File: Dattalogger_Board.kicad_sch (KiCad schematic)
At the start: 0 parts

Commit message: Have added required symbols to the schematic sheets.
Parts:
- added BT1: Battery, Connector_PinHeader_2.54mm:PinHeader_2x01_P2.54mm_Vertical, symbol Device:Battery
- added C1, C2, C3, C4: C, Capacitor_SMD:C_0805_2012Metric, symbol Device:C
- added C5: C_Polarized, symbol Device:C_Polarized
- added D1, D2: LED, LED_SMD:LED_0805_2012Metric, symbol Device:LED
- added R1, R2, R6: 10K, symbol Device:R
- added R3, R4: 4.7K, symbol Device:R
- added R5, R7: 330, symbol Device:R
- added U1: ATMEGA328P-AU, ATMEGA328P-AU:QFP80P900X900X120-32N, symbol ATMEGA328P-AU:ATMEGA328P-AU
- added U2: RV-3129-C3, RV-3129-C3:IC_RV-3129-C3, symbol RV-3129-C3:RV-3129-C3
- added U3, U4: 24LC1025, Package_SO:SOIC-8_5.23x5.23mm_P1.27mm, symbol Memory_EEPROM:24LC1025
- added Y1: 32.768 KHz, CC7V-T1A-100.000KHZ-9PF-100PPM-TA-QC:XTAL_CC7V-T1A-100.000KHZ-9PF-100PPM-TA-QC, symbol CC7V-T1A-100.000KHZ-9PF-100PPM-TA-QC:CC7V-T1A-100.000KHZ-9PF-100PPM-TA-QC
- added Y2: 16 MHz, CC7V-T1A-100.000KHZ-9PF-100PPM-TA-QC:XTAL_CC7V-T1A-100.000KHZ-9PF-100PPM-TA-QC, symbol CC7V-T1A-100.000KHZ-9PF-100PPM-TA-QC:CC7V-T1A-100.000KHZ-9PF-100PPM-TA-QC
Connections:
- new net: U2.10 (NC), U2.8 (NC)
- new net: U1.21 (GND), U1.3 (GND), U1.5 (GND)
- new net: U1.4 (VCC), U1.6 (VCC)
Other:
- added sheet Connectors (Connectors.kicad_sch)

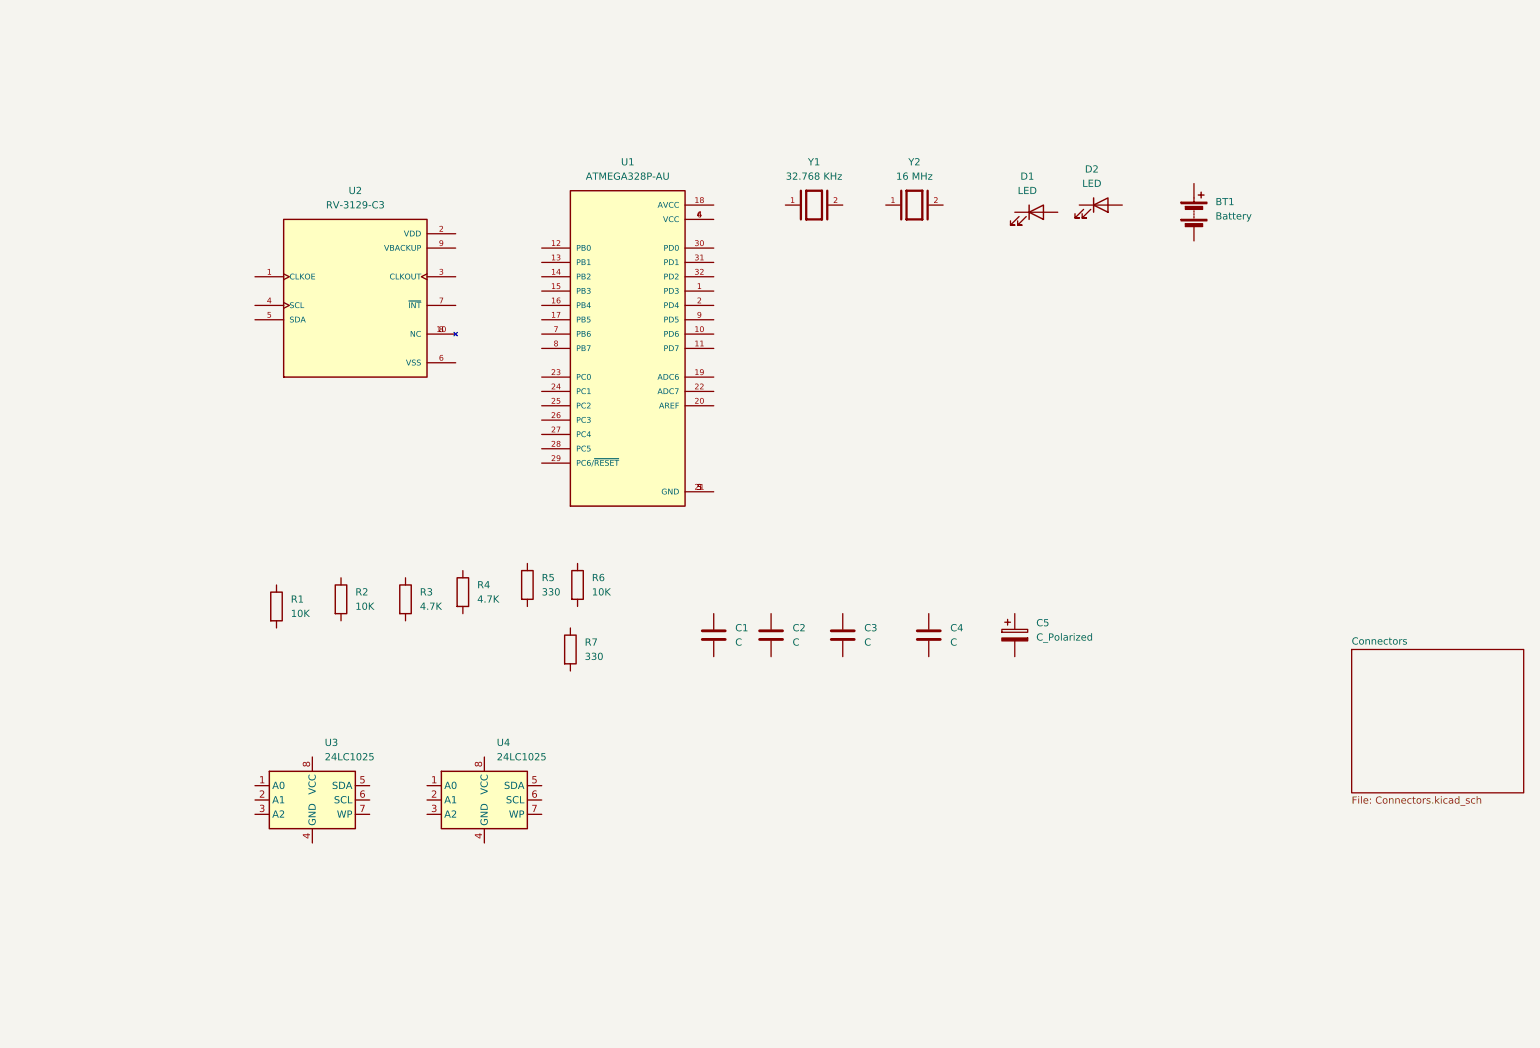
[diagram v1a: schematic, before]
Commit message: Changed Locations of Symbols (arrange).
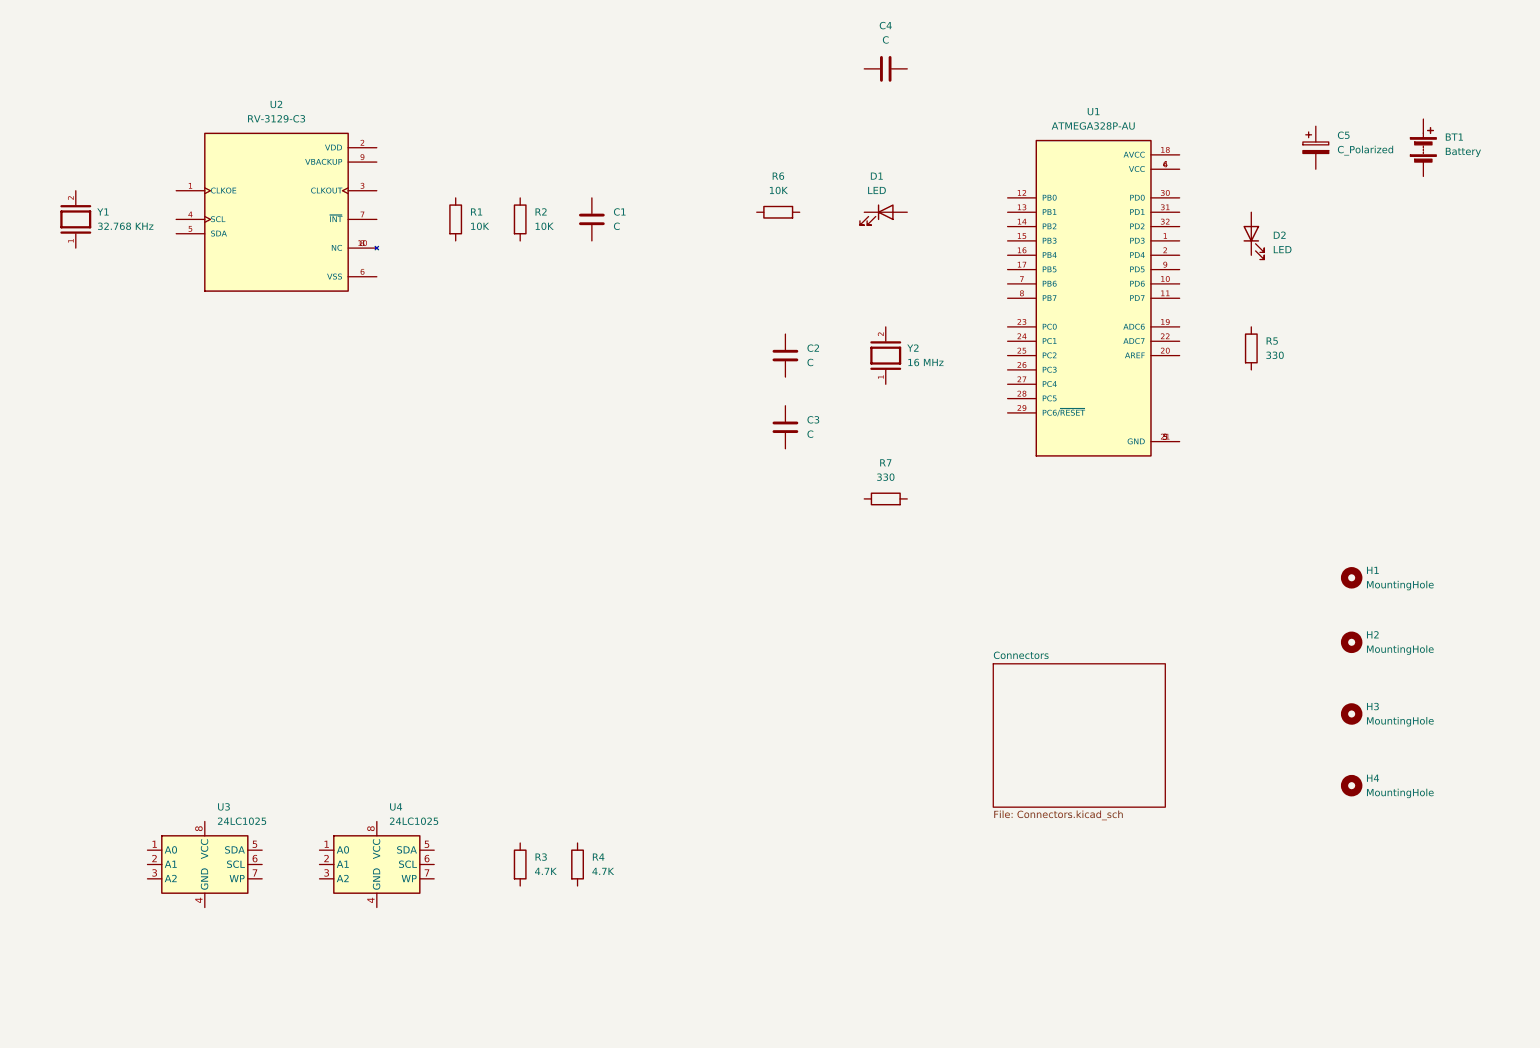
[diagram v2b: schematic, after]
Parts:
- added H1, H2, H3, H4: MountingHole, symbol Mechanical:MountingHole
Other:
- moved on the sheet: BT1, C1, C2, C3, C4, C5, D1, D2, R1, R2, R3, R4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

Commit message: Added Components Values
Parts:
- C1, C4: value C -> 0.1uF
- C2, C3: value C -> 22pF
- C5: value C_Polarized -> 100nF; footprint (none) -> Capacitor_SMD:C_0805_2012Metric
- H1, H2, H3, H4: footprint (none) -> MountingHole:MountingHole_2.1mm
- R1, R2, R3, R4, R5, R6, R7: footprint (none) -> Resistor_SMD:R_0805_2012Metric
- U2: footprint RV-3129-C3:IC_RV-3129-C3 -> Library:IC_RV-3129-C3
- Y1, Y2: footprint CC7V-T1A-100.000KHZ-9PF-100PPM-TA-QC:XTAL_CC7V-T1A-100.000KHZ-9PF-100PPM-TA-QC -> Crystal:Crystal_SMD_5032-2Pin_5.0x3.2mm_HandSoldering
- renumbered U4 to U1, U1 to U4
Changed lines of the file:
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@@
       (effects (font (size 1.27 1.27)) (justify left))
     )
-    (property "Value" "C" (at 157.48 88.9 0)
+    (property "Value" "22pF" (at 157.48 88.9 0)
       (effects (font (size 1.27 1.27)) (justify left))
     )
@@
       (effects (font (size 1.27 1.27)))
     )
-    (property "Footprint" "" (at 171.45 102.108 90)
+    (property "Footprint" "Resistor_SMD:R_0805_2012Metric" (at 171.45 102.108 90)
       (effects (font (size 1.27 1.27)) hide)
     )
@@
       (effects (font (size 1.27 1.27)))
     )
-    (property "Footprint" "" (at 152.4 51.308 90)
+    (property "Footprint" "Resistor_SMD:R_0805_2012Metric" (at 152.4 51.308 90)
       (effects (font (size 1.27 1.27)) hide)
     )
@@
       (effects (font (size 1.27 1.27)) (justify left))
     )
-    (property "Footprint" "" (at 254 151.13 0)
+    (property "Footprint" "MountingHole:MountingHole_2.1mm" (at 254 151.13 0)
       (effects (font (size 1.27 1.27)) hide)
     )
@@
       (effects (font (size 1.27 1.27)) (justify left))
     )
-    (property "Footprint" "" (at 104.902 50.8 90)
+    (property "Footprint" "Resistor_SMD:R_0805_2012Metric" (at 104.902 50.8 90)
       (effects (font (size 1.27 1.27)) hide)
     )
@@
       (effects (font (size 1.27 1.27)) (justify left))
     )
-    (property "Footprint" "" (at 254 114.3 0)
+    (property "Footprint" "MountingHole:MountingHole_2.1mm" (at 254 114.3 0)
       (effects (font (size 1.27 1.27)) hide)
     )
@@
       (effects (font (size 1.27 1.27)) (justify left))
     )
-    (property "Footprint" "" (at 254 138.43 0)
+    (property "Footprint" "MountingHole:MountingHole_2.1mm" (at 254 138.43 0)
       (effects (font (size 1.27 1.27)) hide)
     )
@@
       (effects (font (size 1.27 1.27)))
     )
-    (property "Value" "C" (at 171.45 19.05 90)
+    (property "Value" "0.1uF" (at 171.45 19.05 90)
       (effects (font (size 1.27 1.27)))
     )
@@
       (effects (font (size 1.27 1.27)) (justify left))
     )
-    (property "Footprint" "" (at 93.472 50.8 90)
+    (property "Footprint" "Resistor_SMD:R_0805_2012Metric" (at 93.472 50.8 90)
       (effects (font (size 1.27 1.27)) hide)
     )
@@
       (effects (font (size 1.27 1.27)) (justify left))
     )
-    (property "Footprint" "" (at 234.442 73.66 90)
+    (property "Footprint" "Resistor_SMD:R_0805_2012Metric" (at 234.442 73.66 90)
       (effects (font (size 1.27 1.27)) hide)
     )
@@
       (effects (font (size 1.27 1.27)))
     )
-    (property "Footprint" "RV-3129-C3:IC_RV-3129-C3" (at 63.5 50.8 0)
+    (property "Footprint" "Library:IC_RV-3129-C3" (at 63.5 50.8 0)
       (effects (font (size 1.27 1.27)) (justify bottom) hide)
     )
@@
     (property "Check_prices" "https://www.snapeda.com/parts/RV-3129-C3-32.768KHZ-OPTION-A-TA-QC-T3/Micro+Crystal+AG/view-part/?ref=eda" (at 63.5 50.8 0)
       (effects (font (size 1.27 1.27)) (justify bottom) hide)
+    )
+    (property "Purpose" "" (at 63.5 50.8 0)
+      (effects (font (size 1.27 1.27)))
     )
     (pin "5")
@@
       (effects (font (size 1.27 1.27)) (justify left))
     )
-    (property "Footprint" "" (at 104.902 165.1 90)
+    (property "Footprint" "Resistor_SMD:R_0805_2012Metric" (at 104.902 165.1 90)
       (effects (font (size 1.27 1.27)) hide)
     )
@@
       (effects (font (size 1.27 1.27)) (justify left))
     )
-    (property "Value" "C_Polarized" (at 251.46 38.481 0)
-      (effects (font (size 1.27 1.27)) (justify left))
-    )
-    (property "Footprint" "" (at 248.6152 41.91 0)
+    (property "Value" "100nF" (at 251.46 38.481 0)
+      (effects (font (size 1.27 1.27)) (justify left))
+    )
+    (property "Footprint" "Capacitor_SMD:C_0805_2012Metric" (at 248.6152 41.91 0)
       (effects (font (size 1.27 1.27)) hide)
     )
@@
       (effects (font (size 1.27 1.27)) (justify right))
     )
-    (property "Footprint" "CC7V-T1A-100.000KHZ-9PF-100PPM-TA-QC:XTAL_CC7V-T1A-100.000KHZ-9PF-100PPM-TA-QC" (at 27.94 50.8 0)
+    (property "Footprint" "Crystal:Crystal_SMD_5032-2Pin_5.0x3.2mm_HandSoldering" (at 27.94 50.8 0)
       (effects (font (size 1.27 1.27)) (justify bottom) hide)
     )
@@
       (effects (font (size 1.27 1.27)) (justify left))
     )
-    (property "Value" "C" (at 123.19 52.07 0)
+    (property "Value" "0.1uF" (at 123.19 52.07 0)
       (effects (font (size 1.27 1.27)) (justify left))
     )
@@
   (symbol (lib_id "ATMEGA328P-AU:ATMEGA328P-AU") (at 208.28 64.77 0) (unit 1)
     (in_bom yes) (on_board yes) (dnp no) (fields_autoplaced)
-    (property "Reference" "U1" (at 208.28 31.75 0)
+    (property "Reference" "U4" (at 208.28 31.75 0)
       (effects (font (size 1.27 1.27)))
     )
@@
     (property "MANUFACTURER" "Microchip" (at 208.28 64.77 0)
       (effects (font (size 1.27 1.27)) (justify bottom) hide)
+    )
+    (property "Purpose" "" (at 208.28 64.77 0)
+      (effects (font (size 1.27 1.27)))
     )
     (pin "1")
@@
       (project "Dattalogger_Board"
         (path "/a55893b1-5494-496a-9815-de4061e18fde"
-          (reference "U1") (unit 1)
+          (reference "U4") (unit 1)
         )
       )
@@
       (effects (font (size 1.27 1.27)) (justify left))
     )
-    (property "Footprint" "" (at 254 125.73 0)
+    (property "Footprint" "MountingHole:MountingHole_2.1mm" (at 254 125.73 0)
       (effects (font (size 1.27 1.27)) hide)
     )
@@
   (symbol (lib_id "Memory_EEPROM:24LC1025") (at 81.28 165.1 0) (unit 1)
     (in_bom yes) (on_board yes) (dnp no) (fields_autoplaced)
-    (property "Reference" "U4" (at 83.4741 154.94 0)
+    (property "Reference" "U1" (at 83.4741 154.94 0)
       (effects (font (size 1.27 1.27)) (justify left))
     )
@@
       (project "Dattalogger_Board"
         (path "/a55893b1-5494-496a-9815-de4061e18fde"
-          (reference "U4") (unit 1)
+          (reference "U1") (unit 1)
         )
       )
@@
       (effects (font (size 1.27 1.27)) (justify left))
     )
-    (property "Footprint" "" (at 115.062 165.1 90)
+    (property "Footprint" "Resistor_SMD:R_0805_2012Metric" (at 115.062 165.1 90)
       (effects (font (size 1.27 1.27)) hide)
     )
@@
       (effects (font (size 1.27 1.27)) (justify right))
     )
-    (property "Footprint" "CC7V-T1A-100.000KHZ-9PF-100PPM-TA-QC:XTAL_CC7V-T1A-100.000KHZ-9PF-100PPM-TA-QC" (at 171.45 74.93 0)
+    (property "Footprint" "Crystal:Crystal_SMD_5032-2Pin_5.0x3.2mm_HandSoldering" (at 171.45 74.93 0)
       (effects (font (size 1.27 1.27)) (justify bottom) hide)
     )
@@
       (effects (font (size 1.27 1.27)) (justify left))
     )
-    (property "Value" "C" (at 157.48 76.2 0)
-      (effects (font (size 1.27 1.27)) (justify left))
-    )
+    (property "Value" "22pF" (at 157.48 76.2 0)
+      (effects (font (size 1.27 1.27)) (justify left))
+    )

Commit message: More footprint assignment
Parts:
- removed U2: RV-3129-C3, Library:IC_RV-3129-C3, symbol RV-3129-C3:RV-3129-C3
- added U2: DS1337S_, Project_Libraries:SOIC127P600X175-8N, symbol DS1337S_:DS1337S_
- U4: footprint ATMEGA328P-AU:QFP80P900X900X120-32N -> Project_Libraries:QFP80P900X900X120-32N
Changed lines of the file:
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@@
-    )
-  )
-  (symbol (lib_id "RV-3129-C3:RV-3129-C3") (at 63.5 50.8 0) (unit 1)
-    (in_bom yes) (on_board yes) (dnp no) (fields_autoplaced)
-    (property "Reference" "U2" (at 63.5 30.48 0)
-      (effects (font (size 1.27 1.27)))
-    )
-    (property "Value" "RV-3129-C3" (at 63.5 33.02 0)
-      (effects (font (size 1.27 1.27)))
-    )
-    (property "Footprint" "Library:IC_RV-3129-C3" (at 63.5 50.8 0)
-      (effects (font (size 1.27 1.27)) (justify bottom) hide)
-    )
-    (property "Datasheet" "" (at 63.5 50.8 0)
-      (effects (font (size 1.27 1.27)) hide)
-    )
-    (property "SnapEDA_Link" "https://www.snapeda.com/parts/RV-3129-C3-32.768KHZ-OPTION-A-TA-QC-T3/Micro+Crystal+AG/view-part/?ref=snap" (at 63.5 50.8 0)
-      (effects (font (size 1.27 1.27)) (justify bottom) hide)
-    )
-    (property "Description" "\nReal Time Clock (RTC) IC Clock/Calendar 8B I2C, 2-Wire Serial 10-VCDFN\n" (at 63.5 50.8 0)
-      (effects (font (size 1.27 1.27)) (justify bottom) hide)
-    )
-    (property "Package" "QFN-10 Micro Crystal" (at 63.5 50.8 0)
-      (effects (font (size 1.27 1.27)) (justify bottom) hide)
-    )
-    (property "Price" "None" (at 63.5 50.8 0)
-      (effects (font (size 1.27 1.27)) (justify bottom) hide)
-    )
-    (property "MF" "Micro Crystal AG" (at 63.5 50.8 0)
-      (effects (font (size 1.27 1.27)) (justify bottom) hide)
-    )
-    (property "MP" "RV-3129-C3-32.768KHZ-OPTION-A-TA-QC-T3" (at 63.5 50.8 0)
-      (effects (font (size 1.27 1.27)) (justify bottom) hide)
-    )
-    (property "Purchase-URL" "https://www.snapeda.com/api/url_track_click_mouser/?unipart_id=15537135&manufacturer=Micro Crystal AG&part_name=RV-3129-C3-32.768KHZ-OPTION-A-TA-QC-T3&search_term=ds1337s" (at 63.5 50.8 0)
-      (effects (font (size 1.27 1.27)) (justify bottom) hide)
-    )
-    (property "Availability" "In Stock" (at 63.5 50.8 0)
-      (effects (font (size 1.27 1.27)) (justify bottom) hide)
-    )
-    (property "Check_prices" "https://www.snapeda.com/parts/RV-3129-C3-32.768KHZ-OPTION-A-TA-QC-T3/Micro+Crystal+AG/view-part/?ref=eda" (at 63.5 50.8 0)
-      (effects (font (size 1.27 1.27)) (justify bottom) hide)
-    )
-    (property "Purpose" "" (at 63.5 50.8 0)
-      (effects (font (size 1.27 1.27)))
-    )
-    (pin "5")
-    (pin "8")
-    (pin "1")
-    (pin "6")
-    (pin "10")
-    (pin "2")
-    (pin "4")
-    (pin "3")
-    (pin "7")
-    (pin "9")
-    (instances
-      (project "Dattalogger_Board"
-        (path "/a55893b1-5494-496a-9815-de4061e18fde"
-          (reference "U2") (unit 1)
-        )
-      )
     )
   )
@@
       (effects (font (size 1.27 1.27)))
     )
-    (property "Footprint" "ATMEGA328P-AU:QFP80P900X900X120-32N" (at 208.28 64.77 0)
+    (property "Footprint" "Project_Libraries:QFP80P900X900X120-32N" (at 208.28 64.77 0)
       (effects (font (size 1.27 1.27)) (justify bottom) hide)
     )
@@
         )
       )
+    )
+  )
+  (symbol (lib_id "DS1337S_:DS1337S_") (at 62.23 52.07 0) (unit 1)
+    (in_bom yes) (on_board yes) (dnp no) (fields_autoplaced)
+    (property "Reference" "U2" (at 62.23 31.75 0)
+      (effects (font (size 1.27 1.27)))
+    )
+    (property "Value" "DS1337S_" (at 62.23 34.29 0)
+      (effects (font (size 1.27 1.27)))
+    )
+    (property "Footprint" "Project_Libraries:SOIC127P600X175-8N" (at 62.23 52.07 0)
+      (effects (font (size 1.27 1.27)) (justify bottom) hide)
+    )
+    (property "Datasheet" "" (at 62.23 52.07 0)
+      (effects (font (size 1.27 1.27)) hide)
+    )
+    (property "MF" "Maxim Integrated Products" (at 62.23 52.07 0)
+      (effects (font (size 1.27 1.27)) (justify bottom) hide)
+    )
+    (property "Description" "\nReal Time Clock (RTC) IC Clock/Calendar I2C, 2-Wire Serial 8-SOIC (0.154, 3.90mm Width)\n" (at 62.23 52.07 0)
+      (effects (font (size 1.27 1.27)) (justify bottom) hide)
+    )
+    (property "Package" "None" (at 62.23 52.07 0)
+      (effects (font (size 1.27 1.27)) (justify bottom) hide)
+    )
+    (property "Price" "None" (at 62.23 52.07 0)
+      (effects (font (size 1.27 1.27)) (justify bottom) hide)
+    )
+    (property "SnapEDA_Link" "https://www.snapeda.com/parts/DS1337S+/Analog+Devices/view-part/?ref=snap" (at 62.23 52.07 0)
+      (effects (font (size 1.27 1.27)) (justify bottom) hide)
+    )
+    (property "MP" "DS1337S+" (at 62.23 52.07 0)
+      (effects (font (size 1.27 1.27)) (justify bottom) hide)
+    )
+    (property "Availability" "In Stock" (at 62.23 52.07 0)
+      (effects (font (size 1.27 1.27)) (justify bottom) hide)
+    )
+    (property "Check_prices" "https://www.snapeda.com/parts/DS1337S+/Analog+Devices/view-part/?ref=eda" (at 62.23 52.07 0)
+      (effects (font (size 1.27 1.27)) (justify bottom) hide)
+    )
+    (property "Purpose" "" (at 62.23 52.07 0)
+      (effects (font (size 1.27 1.27)))
+    )
+    (pin "7")
+    (pin "4")
+    (pin "8")
+    (pin "3")
+    (pin "5")
+    (pin "6")
+    (pin "1")
+    (pin "2")
+    (instances
+      (project "Dattalogger_Board"
+        (path "/a55893b1-5494-496a-9815-de4061e18fde"
+          (reference "U2") (unit 1)
+        )
+      )
